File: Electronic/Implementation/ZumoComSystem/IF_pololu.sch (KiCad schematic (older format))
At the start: 41 parts, among them J4 Left, J5 Conn_02x07_Odd_Even, J6 Right, J7 Conn_02x07_Odd_Even, Q10 AO3414, Q11 AO3414, Q12 AO3414, Q13 AO3414, Q6 AO3414, Q7 AO3414, Q8 AO3414, Q9 AO3414, SW3 SW_Push, SW4 SW_Push, SW5 SW_Push

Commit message: Coutouts, BOM, ...
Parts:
- removed Q10, Q12, Q6: AO3414, Package_TO_SOT_SMD:SOT-23, symbol Device:Q_NMOS_GSD
- removed R24, R30, R35: 10k, Resistor_SMD:R_0603_1608Metric_Pad1.05x0.95mm_HandSolder, symbol Device:R
- added C16, C17, C18: 10n, Capacitor_SMD:C_0603_1608Metric_Pad1.05x0.95mm_HandSolder, symbol Device:C
- D10: Manufacturer (none) -> Broadcom Limited; Part-No. (none) -> HSMF-C118
- D7: Manufacturer (none) -> Würth Elektronik; Part-No. (none) -> 150060SS55040
- D8: Manufacturer (none) -> Würth Elektronik; Part-No. (none) -> 150060VS55040
- D9: Manufacturer (none) -> Würth Elektronik; Part-No. (none) -> 150060BS55040
- J4, J6: Manufacturer (none) -> Samtec; Part-No. (none) -> TSM-113-01-T-DV
- J5: Manufacturer (none) -> Samtec; Part-No. (none) -> TSW-107-07-T-D
- J7: Manufacturer (none) -> Samtec; Part-No. (none) -> SSM-107-T-DV-P
- Q10: renamed from Q13; value AO3414 -> SI2302CDS-T1-BE3; Manufacturer (none) -> Vishay / Siliconix; Part-No. (none) -> SI2302CDS-T1-BE3
- Q6: renamed from Q7; value AO3414 -> SI2302CDS-T1-BE3; Manufacturer (none) -> Vishay / Siliconix; Part-No. (none) -> SI2302CDS-T1-BE3
- Q7: renamed from Q8; value AO3414 -> SI2302CDS-T1-BE3; Manufacturer (none) -> Vishay / Siliconix; Part-No. (none) -> SI2302CDS-T1-BE3
- Q8: renamed from Q9; value AO3414 -> SI2302CDS-T1-BE3; Manufacturer (none) -> Vishay / Siliconix; Part-No. (none) -> SI2302CDS-T1-BE3
- Q9: renamed from Q11; value AO3414 -> SI2302CDS-T1-BE3; Manufacturer (none) -> Vishay / Siliconix; Part-No. (none) -> SI2302CDS-T1-BE3
- R19: renamed from R16; Manufacturer (none) -> YAGEO; Part-No. (none) -> RC0603FR-070RL
- R20: renamed from R17; Manufacturer (none) -> TE Connectivity Passive Product; Part-No. (none) -> CRGCQ0603J10K
- R21: renamed from R18; Manufacturer (none) -> Bourns Inc.; Part-No. (none) -> CR0603-JW-301ELF
- R22: renamed from R19; Manufacturer (none) -> TE Connectivity Passive Product; Part-No. (none) -> CRGCQ0603J10K
- R23: renamed from R20; Manufacturer (none) -> Bourns Inc.; Part-No. (none) -> CR0603-JW-301ELF
- R24: renamed from R21; Manufacturer (none) -> TE Connectivity Passive Product; Part-No. (none) -> CRGCQ0603J10K
- R25: renamed from R22; Manufacturer (none) -> TE Connectivity Passive Product; Part-No. (none) -> RL73N1JR18JTD
- R26: renamed from R23; Manufacturer (none) -> TE Connectivity Passive Product; Part-No. (none) -> CRGCQ0603J10K
- R27: renamed from R25; Manufacturer (none) -> Bourns Inc.; Part-No. (none) -> CR0603-JW-301ELF
- R28: renamed from R26; Manufacturer (none) -> Panasonic Electronic Components; Part-No. (none) -> ERJ-3RSFR15V
- R29: renamed from R27; Manufacturer (none) -> Panasonic Electronic Components; Part-No. (none) -> ERJ-3RSFR15V
- R30: renamed from R28; Manufacturer (none) -> YAGEO; Part-No. (none) -> RC0603FR-070RL
- R31: renamed from R29; Manufacturer (none) -> TE Connectivity Passive Product; Part-No. (none) -> CRGCQ0603J10K
- R32: renamed from R31; Manufacturer (none) -> TE Connectivity Passive Product; Part-No. (none) -> CRGCQ0603J10K
- R33: renamed from R32; Manufacturer (none) -> TE Connectivity Passive Product; Part-No. (none) -> CRGCQ0603J10K
- R34: renamed from R33; Manufacturer (none) -> YAGEO; Part-No. (none) -> RC0603FR-070RL
- R35: renamed from R34; Manufacturer (none) -> TE Connectivity Passive Product; Part-No. (none) -> CRGCQ0603J10K
- R36, R37: Manufacturer (none) -> TE Connectivity Passive Product; Part-No. (none) -> CRGCQ0603J10K
- SW3, SW4, SW5: Manufacturer (none) -> Omron Electronics; Part-No. (none) -> B3U-1000P-B
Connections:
- net GND: now also C16.2, C17.2, C18.2
- net nBUT_A: now also R19.1, R20.2, C16.1
- net nBUT_B: now also R30.1, R31.2, C17.1
- net nBUT_C: now also R34.1, R35.2, C18.1

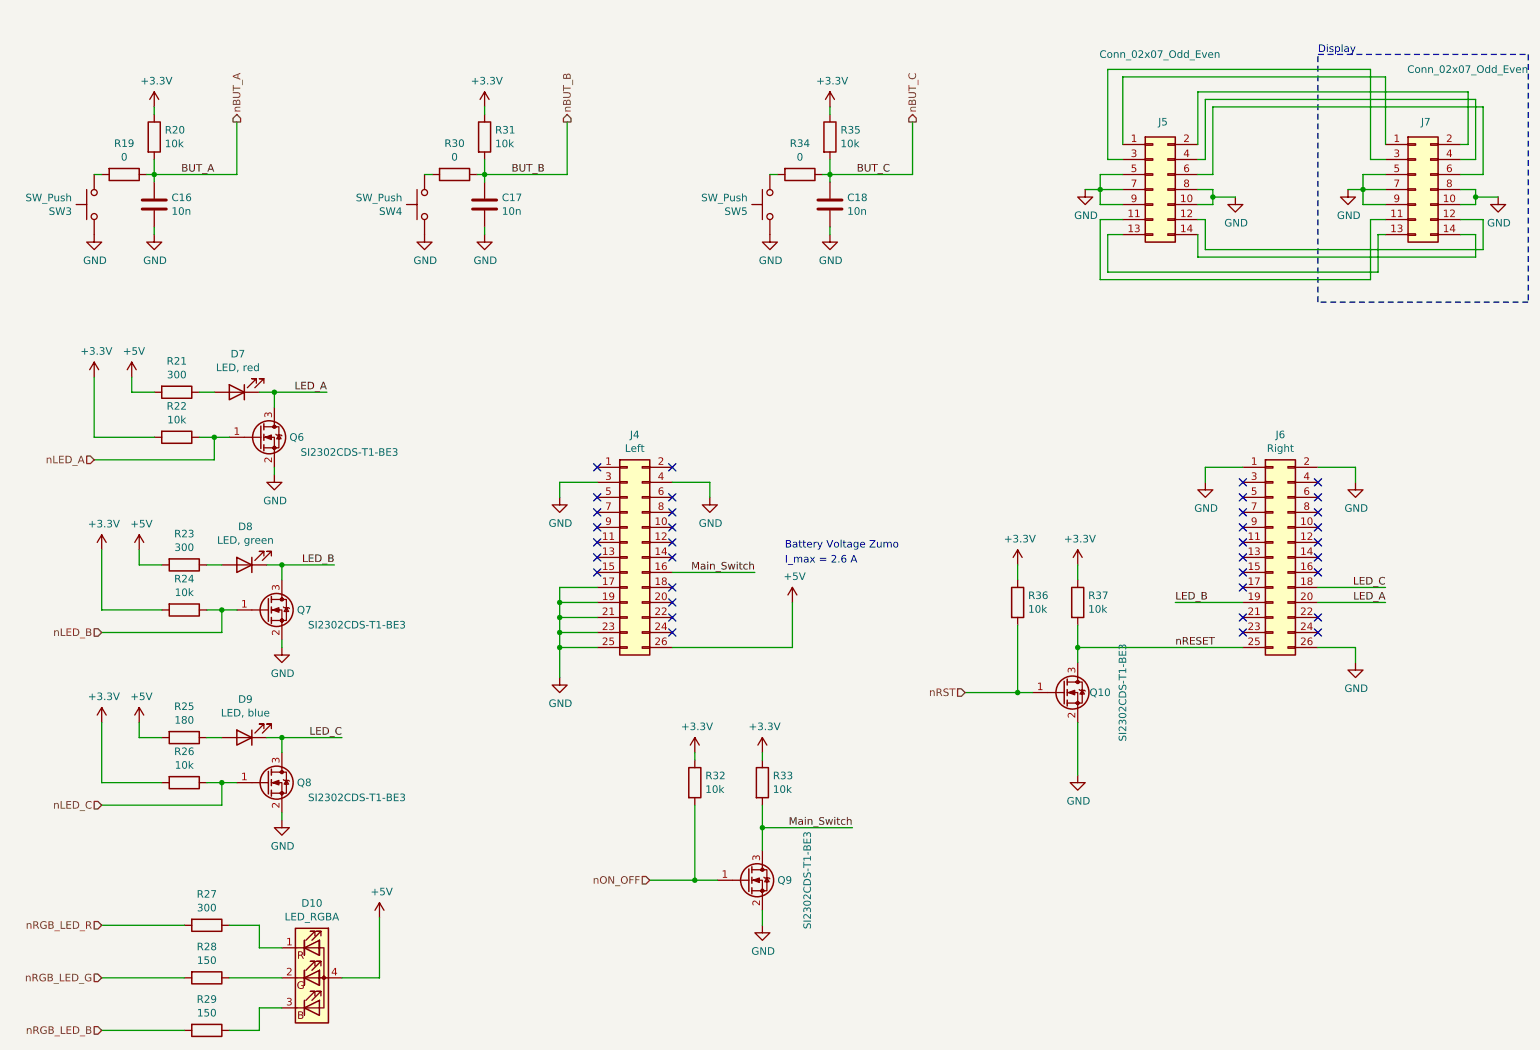
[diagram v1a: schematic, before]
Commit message: replaced 3V3 Regulator
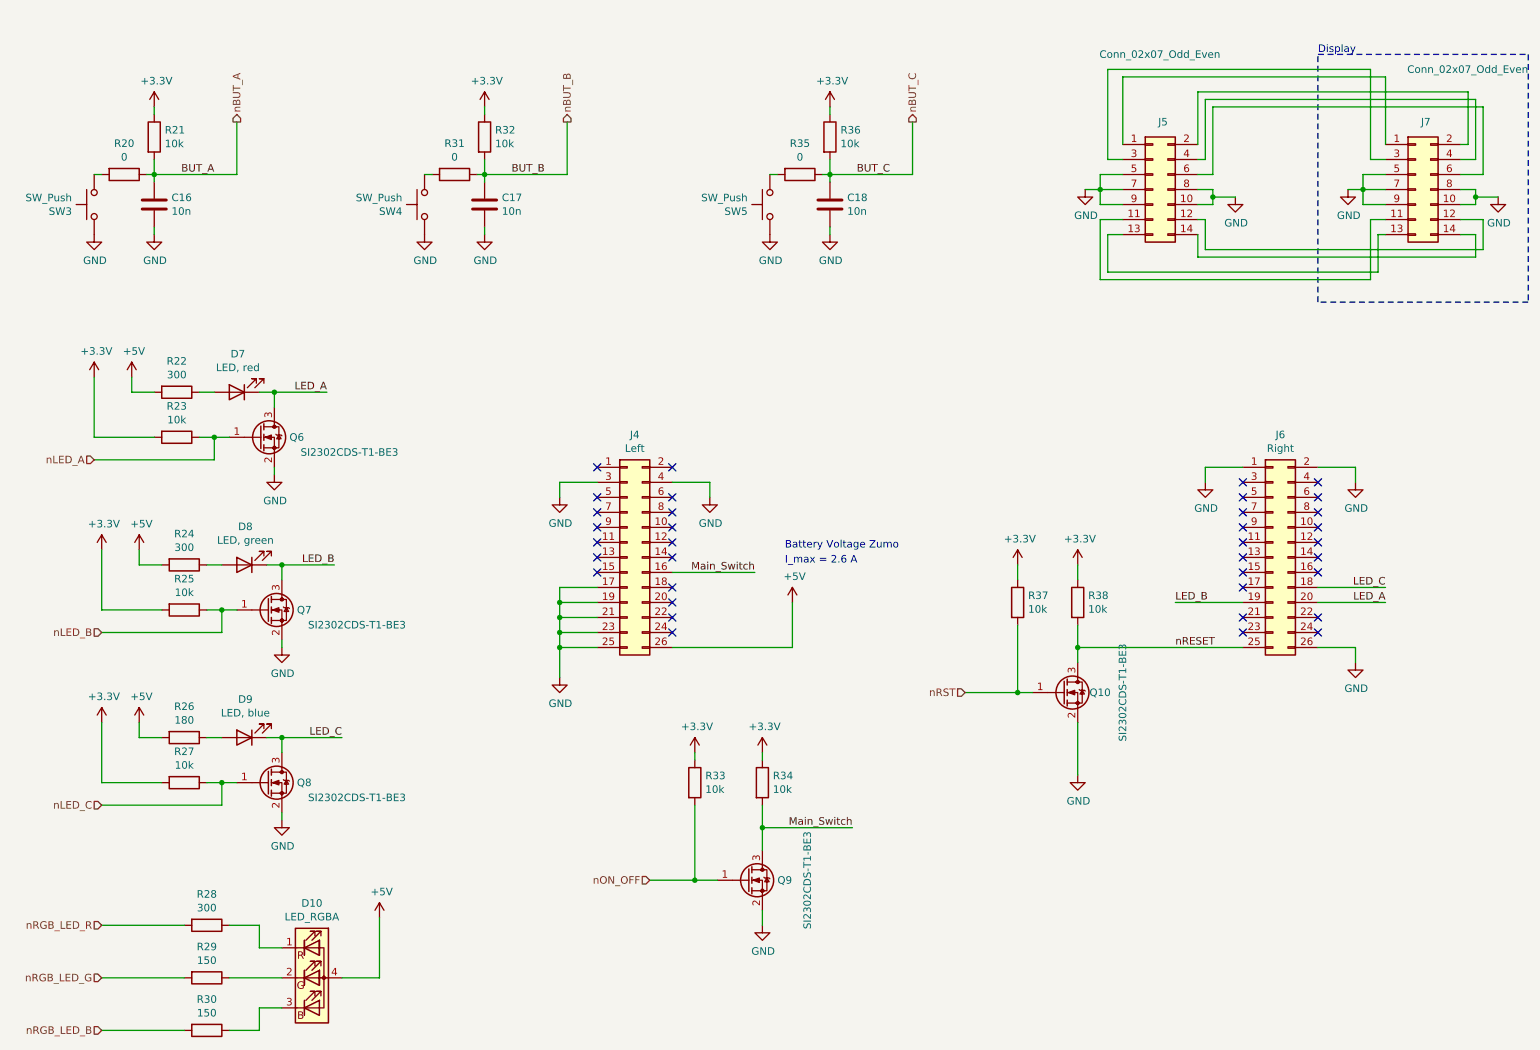
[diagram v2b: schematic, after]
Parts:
- renumbered R19 to R20, R20 to R21, R21 to R22, R22 to R23, R23 to R24, R24 to R25, R25 to R26, R26 to R27, R27 to R28, R28 to R29, R29 to R30, R30 to R31, R31 to R32, R32 to R33, R33 to R34, R34 to R35, R35 to R36, R36 to R37, R37 to R38
